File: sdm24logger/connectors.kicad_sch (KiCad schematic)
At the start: 29 parts, among them J3 USB_B, J4 1-776087-4, J5 1-776087-1, U10 ADR425BRMZ, U11 ADC128S102, U12 SN65HVD230, U13 SN65HVD230, U8 USBLC6-2SC6, U9 TLX9291A

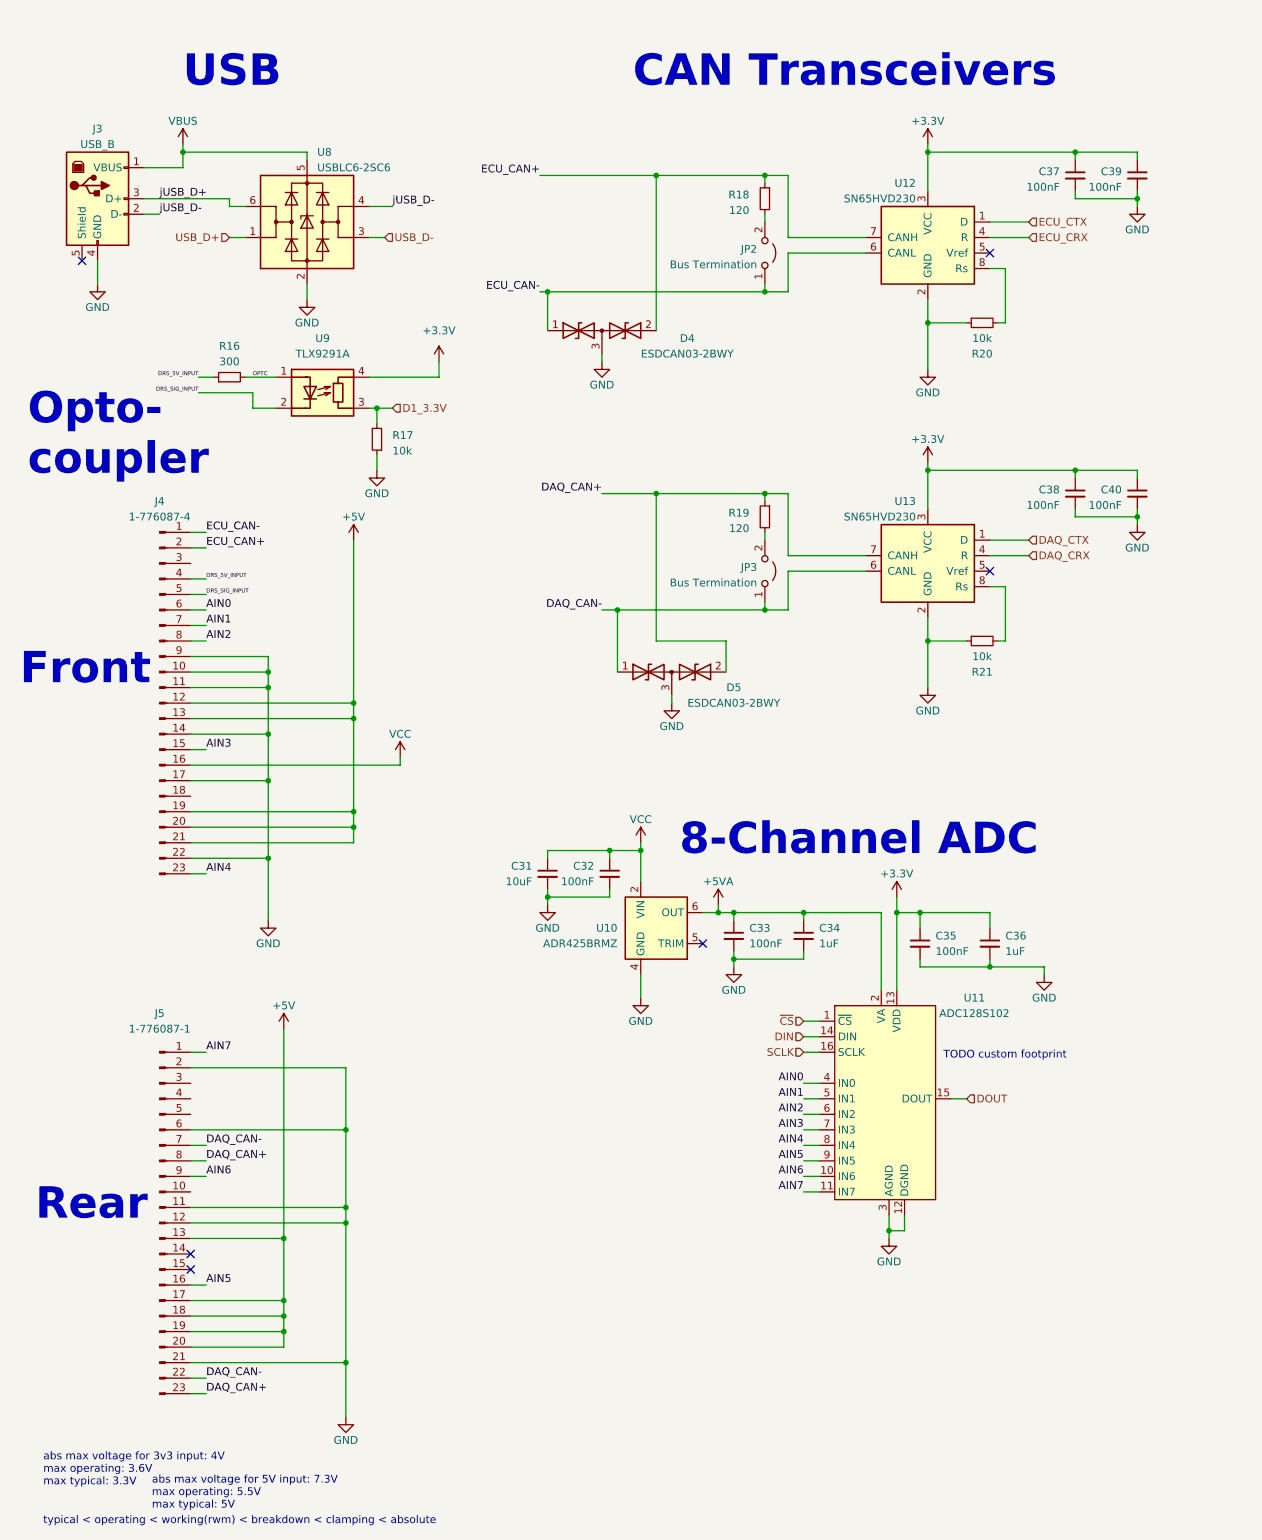
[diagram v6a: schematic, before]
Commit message: sdio routing on data logger
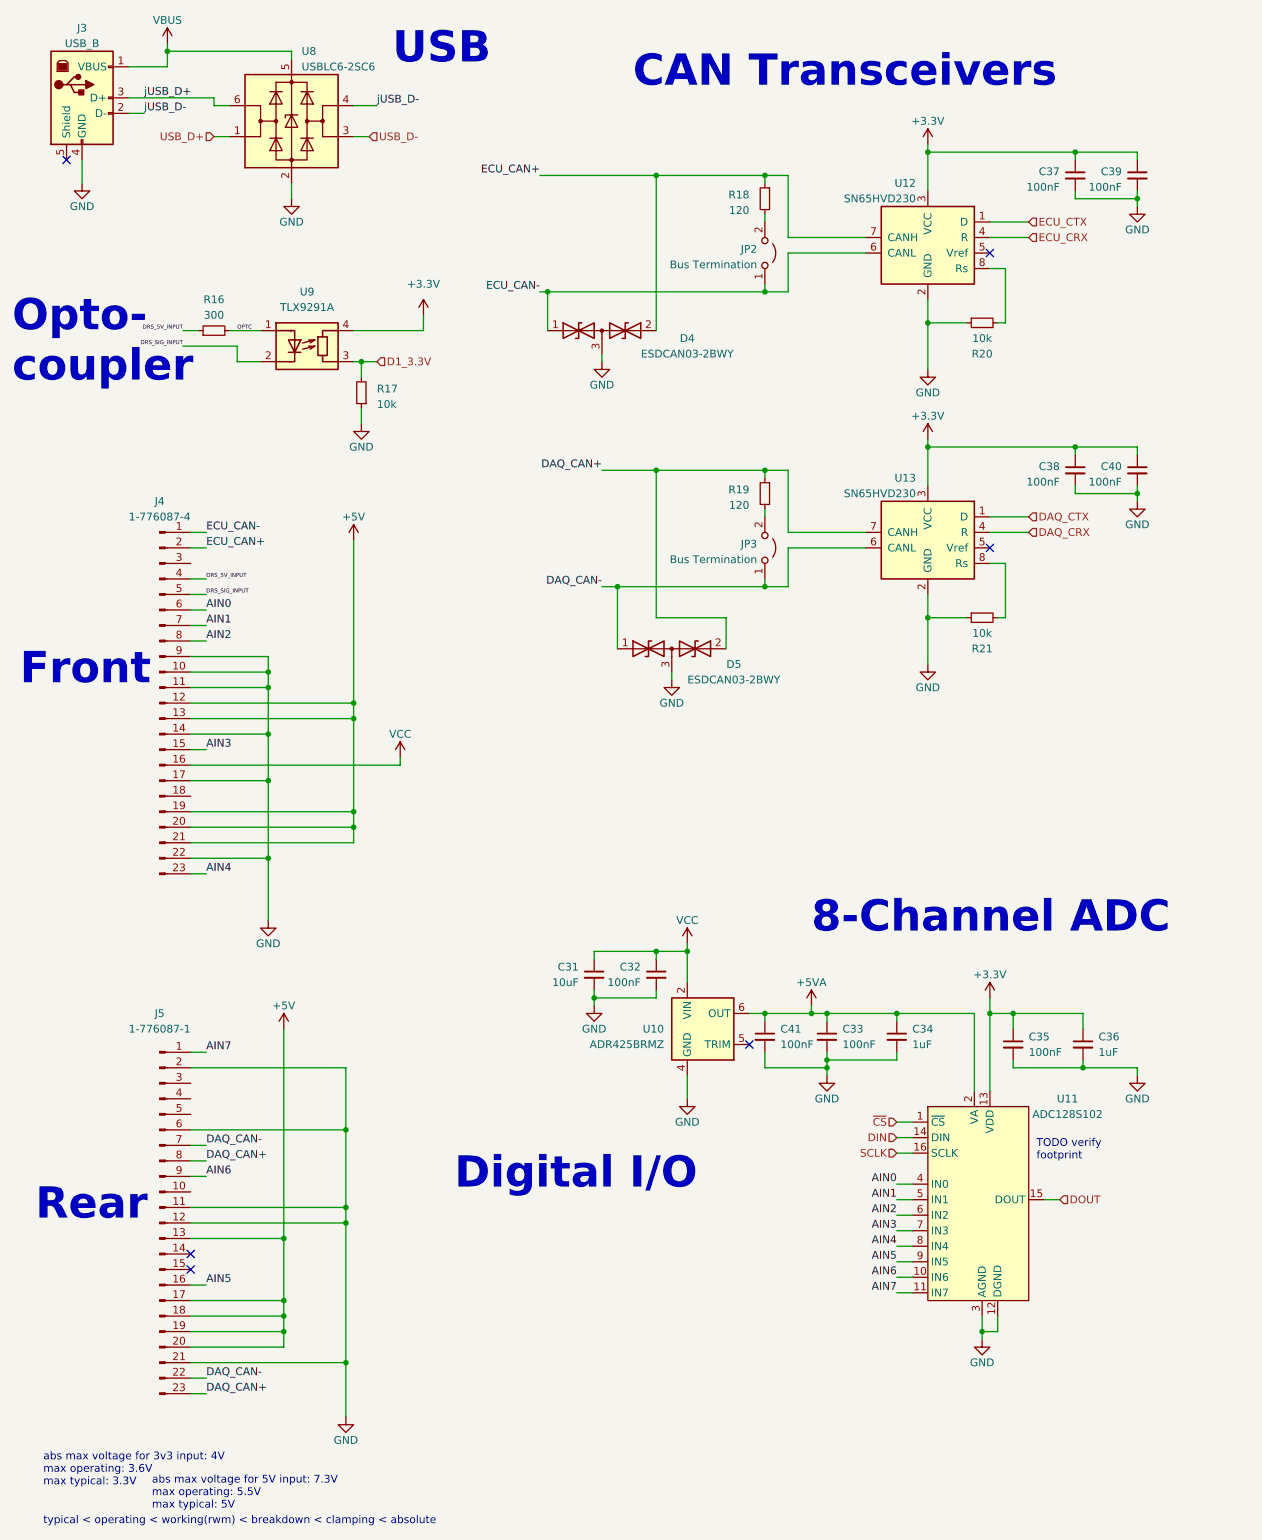
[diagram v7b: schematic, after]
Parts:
- added C41: 100nF, Capacitor_SMD:C_0402_1005Metric, symbol Device:C_Small
- R17: footprint Resistor_SMD:R_0402_1005Metric -> Resistor_SMD:R_0805_2012Metric
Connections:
- net +5VA: now also C41.1
- net GND: now also C41.2
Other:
- note added: "Digital I/O"
- note added: "TODO verify footprint"
- note removed: "TODO custom footprint"
- moved on the sheet: C31, C32, C33, C34, C35, C36, C38, C40, D5, J3, JP3, R16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

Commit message: reorganize logger schematic
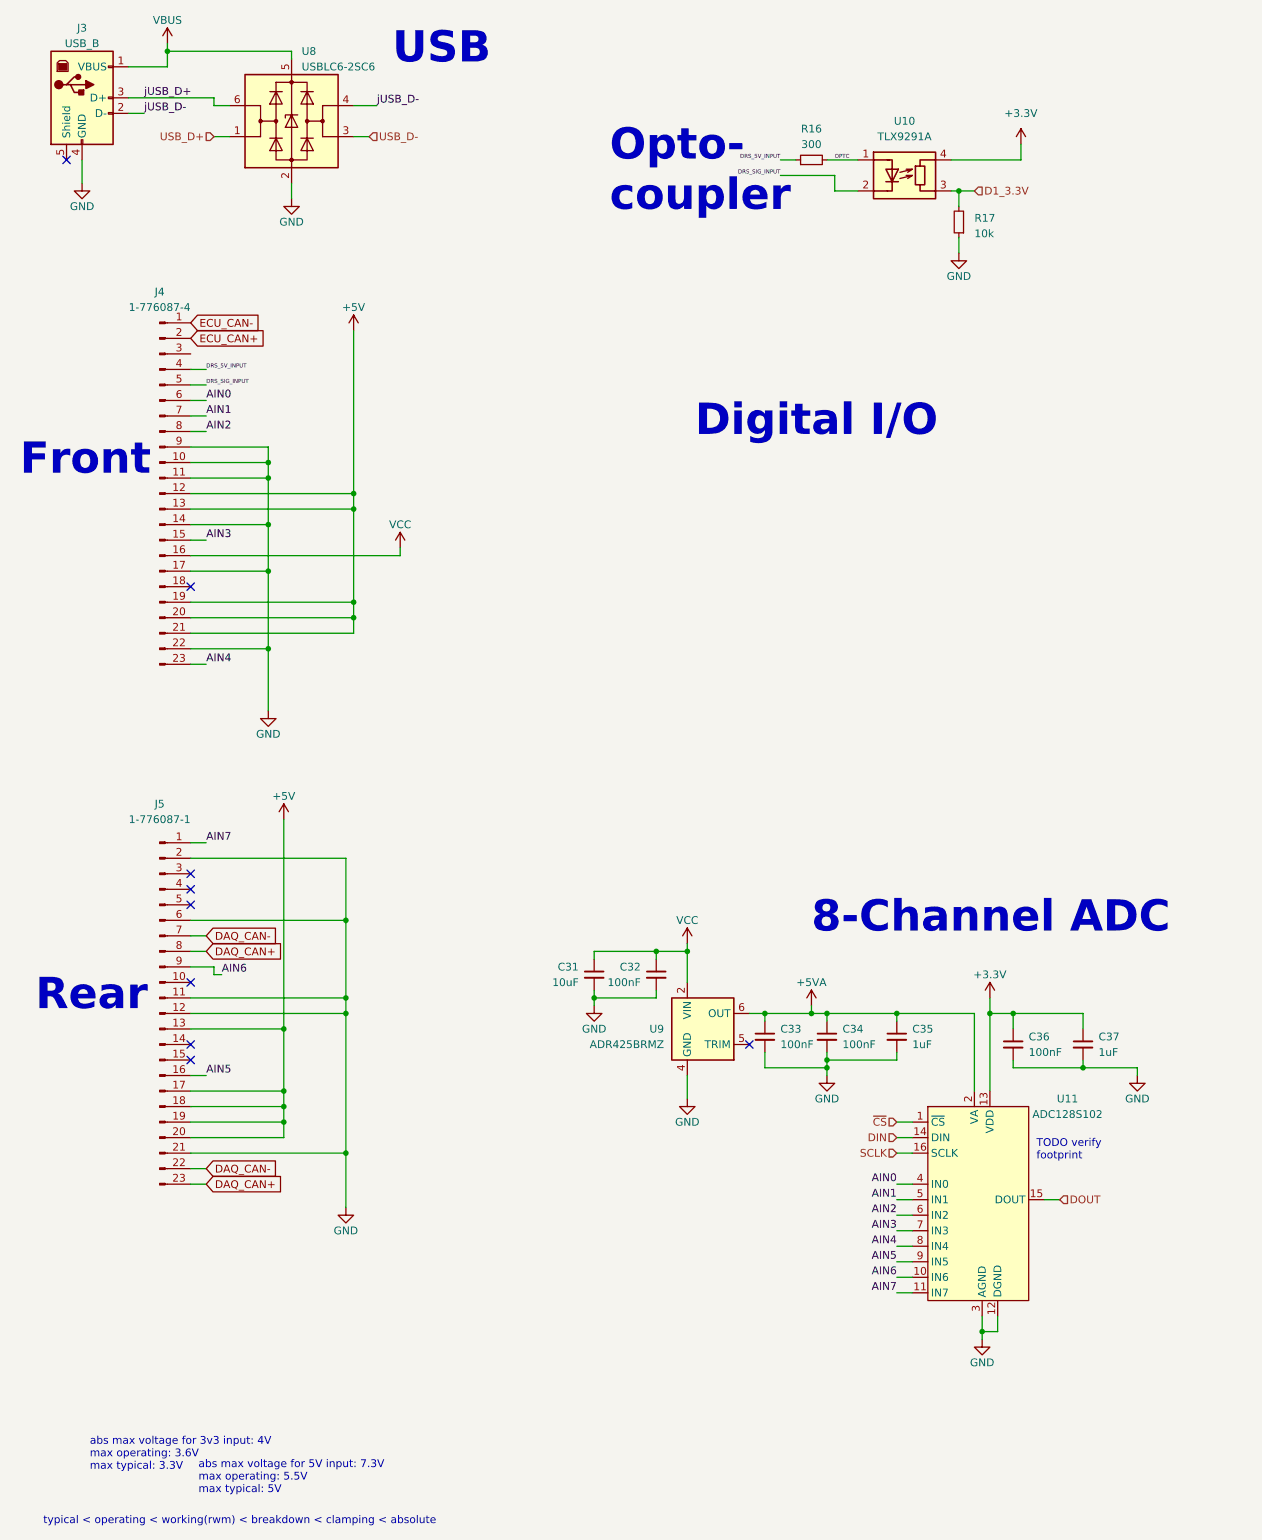
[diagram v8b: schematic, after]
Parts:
- removed C37, C38, C39, C40: 100nF, Capacitor_SMD:C_0402_1005Metric, symbol Device:C_Small
- removed D4, D5: ESDCAN03-2BWY, Package_TO_SOT_SMD:SOT-323_SC-70, symbol Device:D_TVS_Dual_AAC
- removed JP2, JP3: Bus Termination, Connector_PinHeader_2.54mm:PinHeader_1x02_P2.54mm_Vertical, symbol Jumper:Jumper_2_Open
- removed R18, R19: 120, Resistor_SMD:R_0402_1005Metric, symbol Device:R_Small
- removed R20, R21: 10k, Resistor_SMD:R_0603_1608Metric, symbol Device:R_Small
- removed U12, U13: SN65HVD230, Package_SO:SOIC-8_3.9x4.9mm_P1.27mm, symbol Interface_CAN_LIN:SN65HVD230
- renumbered C41 to C33, C33 to C34, C34 to C35, C35 to C36, C36 to C37, U9 to U10, U10 to U9
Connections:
- no-connect marks 6 -> 9
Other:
- note removed: "CAN Transceivers"
- moved on the sheet: J4, J5, R16, R17, U10
